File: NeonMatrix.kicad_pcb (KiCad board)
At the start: 2 copper layers, 86 x 116 mm, 40 parts, among them U1 74HC595, U2 74HC595, U3 74HC595, U4 74HC595, U5 74HC595, U6 74HC595, U7 74HC595, U8 74HC595

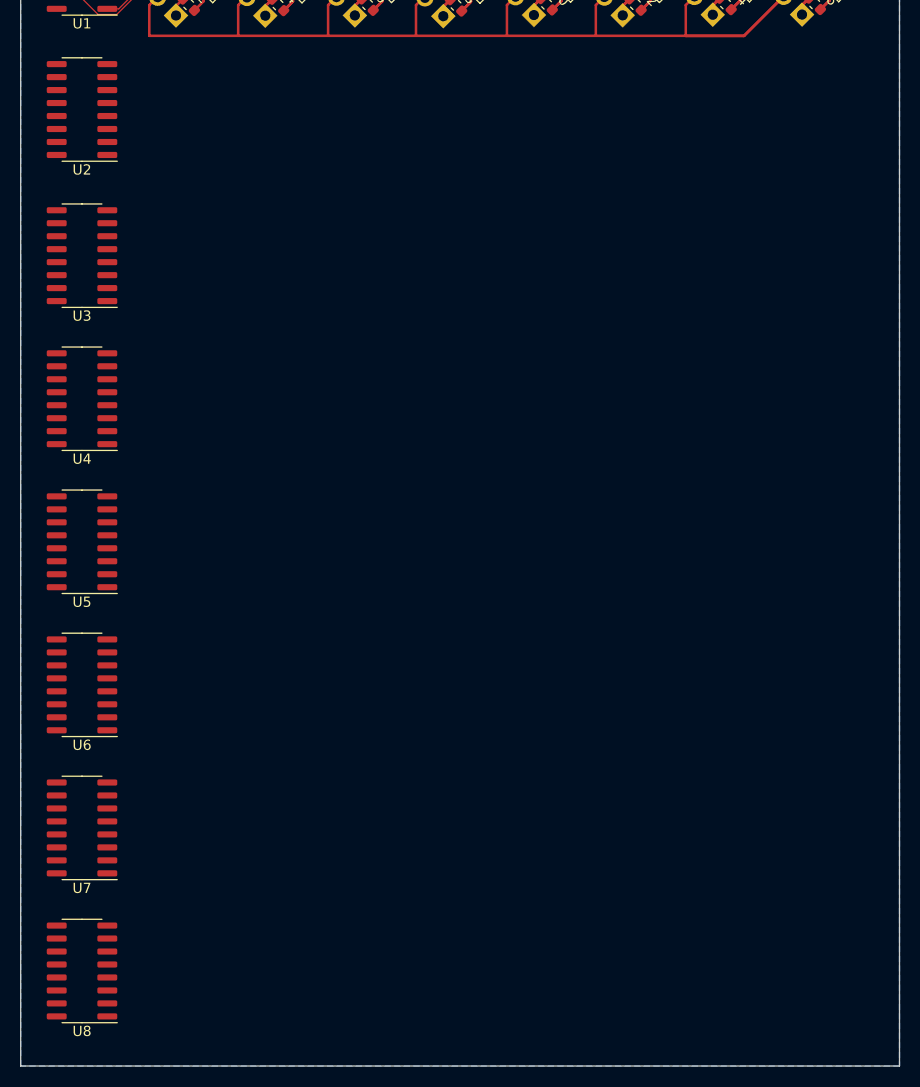
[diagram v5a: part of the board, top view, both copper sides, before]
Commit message: Add isolation
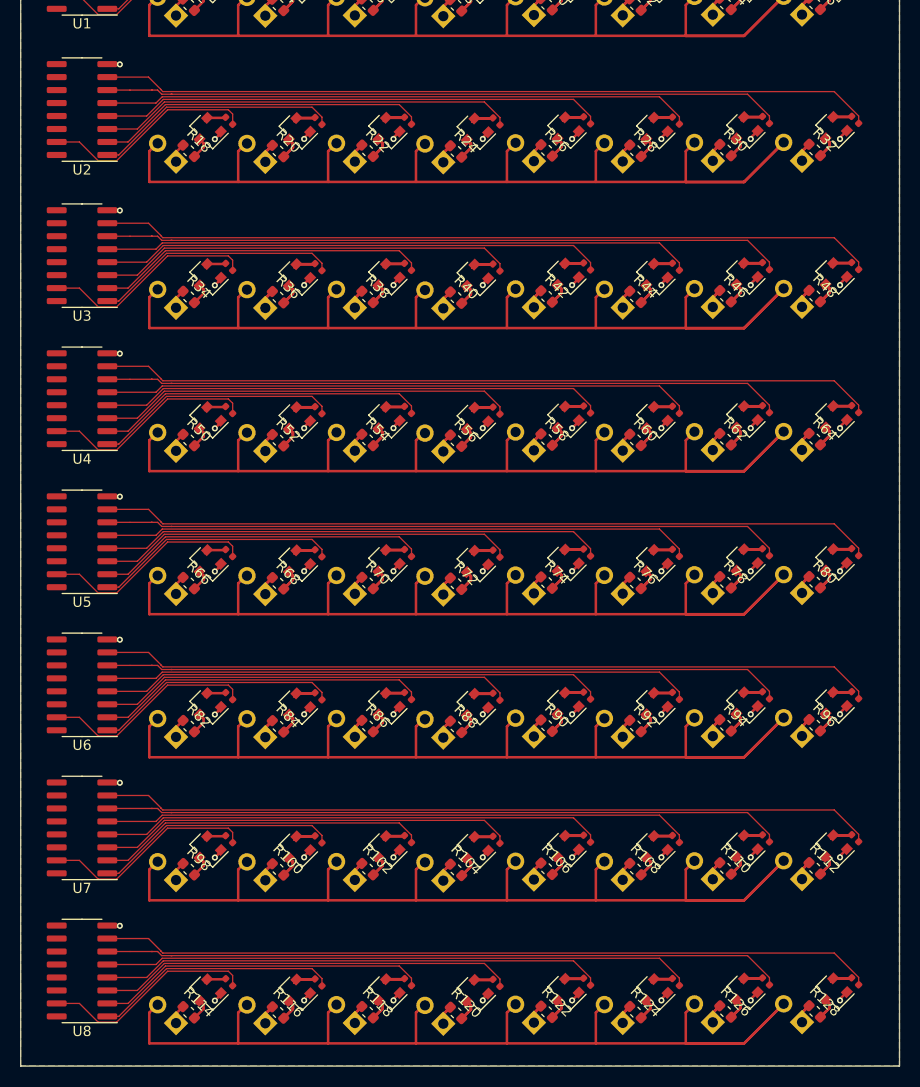
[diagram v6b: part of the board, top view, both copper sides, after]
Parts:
- added D10: Q_TRIAC_A1GA2, Package_TO_SOT_SMD:SOT-23, F.Cu at (48.9, 39.6)
- added D11: Q_TRIAC_A1GA2, Package_TO_SOT_SMD:SOT-23, F.Cu at (57.7, 39.6)
- added D12: Q_TRIAC_A1GA2, Package_TO_SOT_SMD:SOT-23, F.Cu at (66.4, 39.7)
- added D13: Q_TRIAC_A1GA2, Package_TO_SOT_SMD:SOT-23, F.Cu at (75.2, 39.5)
- added D14: Q_TRIAC_A1GA2, Package_TO_SOT_SMD:SOT-23, F.Cu at (83.9, 39.6)
- added D15: Q_TRIAC_A1GA2, Package_TO_SOT_SMD:SOT-23, F.Cu at (92.7, 39.5)
- added D16: Q_TRIAC_A1GA2, Package_TO_SOT_SMD:SOT-23, F.Cu at (101.5, 39.5)
- added D17: Q_TRIAC_A1GA2, Package_TO_SOT_SMD:SOT-23, F.Cu at (40.2, 53.9)
- added D18: Q_TRIAC_A1GA2, Package_TO_SOT_SMD:SOT-23, F.Cu at (48.9, 53.9)
- added D19: Q_TRIAC_A1GA2, Package_TO_SOT_SMD:SOT-23, F.Cu at (57.7, 53.9)
- added D20: Q_TRIAC_A1GA2, Package_TO_SOT_SMD:SOT-23, F.Cu at (66.4, 54.0)
- added D21: Q_TRIAC_A1GA2, Package_TO_SOT_SMD:SOT-23, F.Cu at (75.2, 53.8)
- added D22: Q_TRIAC_A1GA2, Package_TO_SOT_SMD:SOT-23, F.Cu at (83.9, 53.9)
- added D23: Q_TRIAC_A1GA2, Package_TO_SOT_SMD:SOT-23, F.Cu at (92.7, 53.8)
- added D24: Q_TRIAC_A1GA2, Package_TO_SOT_SMD:SOT-23, F.Cu at (101.5, 53.8)
- added D25: Q_TRIAC_A1GA2, Package_TO_SOT_SMD:SOT-23, F.Cu at (40.2, 67.9)
- added D26: Q_TRIAC_A1GA2, Package_TO_SOT_SMD:SOT-23, F.Cu at (48.9, 67.9)
- added D27: Q_TRIAC_A1GA2, Package_TO_SOT_SMD:SOT-23, F.Cu at (57.7, 67.9)
- added D28: Q_TRIAC_A1GA2, Package_TO_SOT_SMD:SOT-23, F.Cu at (66.4, 68.0)
- added D29: Q_TRIAC_A1GA2, Package_TO_SOT_SMD:SOT-23, F.Cu at (75.2, 67.8)
- added D30: Q_TRIAC_A1GA2, Package_TO_SOT_SMD:SOT-23, F.Cu at (83.9, 67.9)
- added D31: Q_TRIAC_A1GA2, Package_TO_SOT_SMD:SOT-23, F.Cu at (92.7, 67.8)
- added D32: Q_TRIAC_A1GA2, Package_TO_SOT_SMD:SOT-23, F.Cu at (101.5, 67.8)
- added D33: Q_TRIAC_A1GA2, Package_TO_SOT_SMD:SOT-23, F.Cu at (40.2, 81.9)
- added D34: Q_TRIAC_A1GA2, Package_TO_SOT_SMD:SOT-23, F.Cu at (48.9, 81.9)
- added D35: Q_TRIAC_A1GA2, Package_TO_SOT_SMD:SOT-23, F.Cu at (57.7, 81.9)
- added D36: Q_TRIAC_A1GA2, Package_TO_SOT_SMD:SOT-23, F.Cu at (66.4, 82.0)
- added D37: Q_TRIAC_A1GA2, Package_TO_SOT_SMD:SOT-23, F.Cu at (75.2, 81.8)
- added D38: Q_TRIAC_A1GA2, Package_TO_SOT_SMD:SOT-23, F.Cu at (83.9, 81.9)
- added D39: Q_TRIAC_A1GA2, Package_TO_SOT_SMD:SOT-23, F.Cu at (92.7, 81.8)
- added D40: Q_TRIAC_A1GA2, Package_TO_SOT_SMD:SOT-23, F.Cu at (101.5, 81.8)
- added D41: Q_TRIAC_A1GA2, Package_TO_SOT_SMD:SOT-23, F.Cu at (40.2, 95.9)
- added D42: Q_TRIAC_A1GA2, Package_TO_SOT_SMD:SOT-23, F.Cu at (48.9, 95.9)
- added D43: Q_TRIAC_A1GA2, Package_TO_SOT_SMD:SOT-23, F.Cu at (57.7, 95.9)
- added D44: Q_TRIAC_A1GA2, Package_TO_SOT_SMD:SOT-23, F.Cu at (66.4, 96.0)
- added D45: Q_TRIAC_A1GA2, Package_TO_SOT_SMD:SOT-23, F.Cu at (75.2, 95.8)
- added D46: Q_TRIAC_A1GA2, Package_TO_SOT_SMD:SOT-23, F.Cu at (83.9, 95.9)
- added D47: Q_TRIAC_A1GA2, Package_TO_SOT_SMD:SOT-23, F.Cu at (92.7, 95.8)
- added D48: Q_TRIAC_A1GA2, Package_TO_SOT_SMD:SOT-23, F.Cu at (101.5, 95.8)
- added D49: Q_TRIAC_A1GA2, Package_TO_SOT_SMD:SOT-23, F.Cu at (40.2, 109.9)
- added D50: Q_TRIAC_A1GA2, Package_TO_SOT_SMD:SOT-23, F.Cu at (48.9, 109.9)
- added D51: Q_TRIAC_A1GA2, Package_TO_SOT_SMD:SOT-23, F.Cu at (57.7, 109.9)
- added D52: Q_TRIAC_A1GA2, Package_TO_SOT_SMD:SOT-23, F.Cu at (66.4, 110.0)
- added D53: Q_TRIAC_A1GA2, Package_TO_SOT_SMD:SOT-23, F.Cu at (75.2, 109.8)
- added D54: Q_TRIAC_A1GA2, Package_TO_SOT_SMD:SOT-23, F.Cu at (83.9, 109.9)
- added D55: Q_TRIAC_A1GA2, Package_TO_SOT_SMD:SOT-23, F.Cu at (92.7, 109.8)
- added D56: Q_TRIAC_A1GA2, Package_TO_SOT_SMD:SOT-23, F.Cu at (101.5, 109.8)
- added D57: Q_TRIAC_A1GA2, Package_TO_SOT_SMD:SOT-23, F.Cu at (40.2, 123.9)
- added D58: Q_TRIAC_A1GA2, Package_TO_SOT_SMD:SOT-23, F.Cu at (48.9, 123.9)
- added D59: Q_TRIAC_A1GA2, Package_TO_SOT_SMD:SOT-23, F.Cu at (57.7, 123.9)
- added D60: Q_TRIAC_A1GA2, Package_TO_SOT_SMD:SOT-23, F.Cu at (66.4, 124.0)
- added D61: Q_TRIAC_A1GA2, Package_TO_SOT_SMD:SOT-23, F.Cu at (75.2, 123.8)
- added D62: Q_TRIAC_A1GA2, Package_TO_SOT_SMD:SOT-23, F.Cu at (83.9, 123.9)
- added D63: Q_TRIAC_A1GA2, Package_TO_SOT_SMD:SOT-23, F.Cu at (92.7, 123.8)
- added D64: Q_TRIAC_A1GA2, Package_TO_SOT_SMD:SOT-23, F.Cu at (101.5, 123.8)
- added D9: Q_TRIAC_A1GA2, Package_TO_SOT_SMD:SOT-23, F.Cu at (40.2, 39.6)
- added NE10: Lamp_Neon, NeonMatrix_Connector:NeonBulb, B.Cu at (45.9, 42.5)
- added NE11: Lamp_Neon, NeonMatrix_Connector:NeonBulb, B.Cu at (54.7, 42.5)
- added NE12: Lamp_Neon, NeonMatrix_Connector:NeonBulb, B.Cu at (63.4, 42.6)
- added NE13: Lamp_Neon, NeonMatrix_Connector:NeonBulb, B.Cu at (72.2, 42.5)
- added NE14: Lamp_Neon, NeonMatrix_Connector:NeonBulb, B.Cu at (80.9, 42.5)
- added NE15: Lamp_Neon, NeonMatrix_Connector:NeonBulb, B.Cu at (89.7, 42.4)
- added NE16: Lamp_Neon, NeonMatrix_Connector:NeonBulb, B.Cu at (98.5, 42.4)
- added NE17: Lamp_Neon, NeonMatrix_Connector:NeonBulb, B.Cu at (37.2, 56.8)
- added NE18: Lamp_Neon, NeonMatrix_Connector:NeonBulb, B.Cu at (45.9, 56.8)
- added NE19: Lamp_Neon, NeonMatrix_Connector:NeonBulb, B.Cu at (54.7, 56.8)
- added NE20: Lamp_Neon, NeonMatrix_Connector:NeonBulb, B.Cu at (63.4, 56.9)
- added NE21: Lamp_Neon, NeonMatrix_Connector:NeonBulb, B.Cu at (72.2, 56.8)
- added NE22: Lamp_Neon, NeonMatrix_Connector:NeonBulb, B.Cu at (80.9, 56.8)
- added NE23: Lamp_Neon, NeonMatrix_Connector:NeonBulb, B.Cu at (89.7, 56.7)
- added NE24: Lamp_Neon, NeonMatrix_Connector:NeonBulb, B.Cu at (98.5, 56.7)
- added NE25: Lamp_Neon, NeonMatrix_Connector:NeonBulb, B.Cu at (37.2, 70.8)
- added NE26: Lamp_Neon, NeonMatrix_Connector:NeonBulb, B.Cu at (45.9, 70.8)
- added NE27: Lamp_Neon, NeonMatrix_Connector:NeonBulb, B.Cu at (54.7, 70.8)
- added NE28: Lamp_Neon, NeonMatrix_Connector:NeonBulb, B.Cu at (63.4, 70.9)
- added NE29: Lamp_Neon, NeonMatrix_Connector:NeonBulb, B.Cu at (72.2, 70.8)
- added NE30: Lamp_Neon, NeonMatrix_Connector:NeonBulb, B.Cu at (80.9, 70.8)
- added NE31: Lamp_Neon, NeonMatrix_Connector:NeonBulb, B.Cu at (89.7, 70.7)
- added NE32: Lamp_Neon, NeonMatrix_Connector:NeonBulb, B.Cu at (98.5, 70.7)
- added NE33: Lamp_Neon, NeonMatrix_Connector:NeonBulb, B.Cu at (37.2, 84.8)
- added NE34: Lamp_Neon, NeonMatrix_Connector:NeonBulb, B.Cu at (45.9, 84.8)
- added NE35: Lamp_Neon, NeonMatrix_Connector:NeonBulb, B.Cu at (54.7, 84.8)
- added NE36: Lamp_Neon, NeonMatrix_Connector:NeonBulb, B.Cu at (63.4, 84.9)
- added NE37: Lamp_Neon, NeonMatrix_Connector:NeonBulb, B.Cu at (72.2, 84.8)
- added NE38: Lamp_Neon, NeonMatrix_Connector:NeonBulb, B.Cu at (80.9, 84.8)
- added NE39: Lamp_Neon, NeonMatrix_Connector:NeonBulb, B.Cu at (89.7, 84.7)
- added NE40: Lamp_Neon, NeonMatrix_Connector:NeonBulb, B.Cu at (98.5, 84.7)
- added NE41: Lamp_Neon, NeonMatrix_Connector:NeonBulb, B.Cu at (37.2, 98.8)
- added NE42: Lamp_Neon, NeonMatrix_Connector:NeonBulb, B.Cu at (45.9, 98.8)
- added NE43: Lamp_Neon, NeonMatrix_Connector:NeonBulb, B.Cu at (54.7, 98.8)
- added NE44: Lamp_Neon, NeonMatrix_Connector:NeonBulb, B.Cu at (63.4, 98.9)
- added NE45: Lamp_Neon, NeonMatrix_Connector:NeonBulb, B.Cu at (72.2, 98.8)
- added NE46: Lamp_Neon, NeonMatrix_Connector:NeonBulb, B.Cu at (80.9, 98.8)
- added NE47: Lamp_Neon, NeonMatrix_Connector:NeonBulb, B.Cu at (89.7, 98.7)
- added NE48: Lamp_Neon, NeonMatrix_Connector:NeonBulb, B.Cu at (98.5, 98.7)
- added NE49: Lamp_Neon, NeonMatrix_Connector:NeonBulb, B.Cu at (37.2, 112.8)
- added NE50: Lamp_Neon, NeonMatrix_Connector:NeonBulb, B.Cu at (45.9, 112.8)
- added NE51: Lamp_Neon, NeonMatrix_Connector:NeonBulb, B.Cu at (54.7, 112.8)
- added NE52: Lamp_Neon, NeonMatrix_Connector:NeonBulb, B.Cu at (63.4, 112.9)
- added NE53: Lamp_Neon, NeonMatrix_Connector:NeonBulb, B.Cu at (72.2, 112.8)
- added NE54: Lamp_Neon, NeonMatrix_Connector:NeonBulb, B.Cu at (80.9, 112.8)
- added NE55: Lamp_Neon, NeonMatrix_Connector:NeonBulb, B.Cu at (89.7, 112.7)
- added NE56: Lamp_Neon, NeonMatrix_Connector:NeonBulb, B.Cu at (98.5, 112.7)
- added NE57: Lamp_Neon, NeonMatrix_Connector:NeonBulb, B.Cu at (37.2, 126.8)
- added NE58: Lamp_Neon, NeonMatrix_Connector:NeonBulb, B.Cu at (45.9, 126.8)
- added NE59: Lamp_Neon, NeonMatrix_Connector:NeonBulb, B.Cu at (54.7, 126.8)
- added NE60: Lamp_Neon, NeonMatrix_Connector:NeonBulb, B.Cu at (63.4, 126.9)
- added NE61: Lamp_Neon, NeonMatrix_Connector:NeonBulb, B.Cu at (72.2, 126.8)
- added NE62: Lamp_Neon, NeonMatrix_Connector:NeonBulb, B.Cu at (80.9, 126.8)
- added NE63: Lamp_Neon, NeonMatrix_Connector:NeonBulb, B.Cu at (89.7, 126.7)
- added NE64: Lamp_Neon, NeonMatrix_Connector:NeonBulb, B.Cu at (98.5, 126.7)
- added NE9: Lamp_Neon, NeonMatrix_Connector:NeonBulb, B.Cu at (37.2, 42.5)
- added R100: 33k, Resistor_SMD:R_0603_1608Metric, F.Cu at (47.2, 111.8)
- added R101: 330k, Resistor_SMD:R_0402_1005Metric, F.Cu at (59.9, 108.8)
- added R102: 33k, Resistor_SMD:R_0603_1608Metric, F.Cu at (55.9, 111.7)
- added R103: 330k, Resistor_SMD:R_0402_1005Metric, F.Cu at (68.6, 108.9)
- added R104: 33k, Resistor_SMD:R_0603_1608Metric, F.Cu at (64.6, 111.8)
- added R105: 330k, Resistor_SMD:R_0402_1005Metric, F.Cu at (77.4, 108.8)
- added R106: 33k, Resistor_SMD:R_0603_1608Metric, F.Cu at (73.5, 111.7)
- added R107: 330k, Resistor_SMD:R_0402_1005Metric, F.Cu at (86.1, 108.8)
- added R108: 33k, Resistor_SMD:R_0603_1608Metric, F.Cu at (82.2, 111.7)
- added R109: 330k, Resistor_SMD:R_0402_1005Metric, F.Cu at (94.9, 108.7)
- added R110: 33k, Resistor_SMD:R_0603_1608Metric, F.Cu at (91.0, 111.7)
- added R111: 330k, Resistor_SMD:R_0402_1005Metric, F.Cu at (103.7, 108.7)
- added R112: 33k, Resistor_SMD:R_0603_1608Metric, F.Cu at (99.7, 111.7)
- added R113: 330k, Resistor_SMD:R_0402_1005Metric, F.Cu at (42.4, 122.8)
- added R114: 33k, Resistor_SMD:R_0603_1608Metric, F.Cu at (38.4, 125.7)
- added R115: 330k, Resistor_SMD:R_0402_1005Metric, F.Cu at (51.1, 122.8)
- added R116: 33k, Resistor_SMD:R_0603_1608Metric, F.Cu at (47.2, 125.8)
- added R117: 330k, Resistor_SMD:R_0402_1005Metric, F.Cu at (59.9, 122.8)
- added R118: 33k, Resistor_SMD:R_0603_1608Metric, F.Cu at (55.9, 125.7)
- added R119: 330k, Resistor_SMD:R_0402_1005Metric, F.Cu at (68.6, 122.9)
- added R120: 33k, Resistor_SMD:R_0603_1608Metric, F.Cu at (64.6, 125.8)
- added R121: 330k, Resistor_SMD:R_0402_1005Metric, F.Cu at (77.4, 122.8)
- added R122: 33k, Resistor_SMD:R_0603_1608Metric, F.Cu at (73.5, 125.7)
- added R123: 330k, Resistor_SMD:R_0402_1005Metric, F.Cu at (86.1, 122.8)
- added R124: 33k, Resistor_SMD:R_0603_1608Metric, F.Cu at (82.2, 125.7)
- added R125: 330k, Resistor_SMD:R_0402_1005Metric, F.Cu at (94.9, 122.7)
- added R126: 33k, Resistor_SMD:R_0603_1608Metric, F.Cu at (91.0, 125.7)
- added R127: 330k, Resistor_SMD:R_0402_1005Metric, F.Cu at (103.7, 122.7)
- added R128: 33k, Resistor_SMD:R_0603_1608Metric, F.Cu at (99.7, 125.7)
- added R17: 330k, Resistor_SMD:R_0402_1005Metric, F.Cu at (42.4, 38.5)
- added R18: 33k, Resistor_SMD:R_0603_1608Metric, F.Cu at (38.4, 41.4)
- added R19: 330k, Resistor_SMD:R_0402_1005Metric, F.Cu at (51.1, 38.5)
- added R20: 33k, Resistor_SMD:R_0603_1608Metric, F.Cu at (47.2, 41.5)
- added R21: 330k, Resistor_SMD:R_0402_1005Metric, F.Cu at (59.9, 38.5)
- added R22: 33k, Resistor_SMD:R_0603_1608Metric, F.Cu at (55.9, 41.4)
- added R23: 330k, Resistor_SMD:R_0402_1005Metric, F.Cu at (68.6, 38.6)
- added R24: 33k, Resistor_SMD:R_0603_1608Metric, F.Cu at (64.6, 41.5)
- added R25: 330k, Resistor_SMD:R_0402_1005Metric, F.Cu at (77.4, 38.5)
- added R26: 33k, Resistor_SMD:R_0603_1608Metric, F.Cu at (73.5, 41.4)
- added R27: 330k, Resistor_SMD:R_0402_1005Metric, F.Cu at (86.1, 38.5)
- added R28: 33k, Resistor_SMD:R_0603_1608Metric, F.Cu at (82.2, 41.4)
- added R29: 330k, Resistor_SMD:R_0402_1005Metric, F.Cu at (94.9, 38.4)
- added R30: 33k, Resistor_SMD:R_0603_1608Metric, F.Cu at (91.0, 41.4)
- added R31: 330k, Resistor_SMD:R_0402_1005Metric, F.Cu at (103.7, 38.4)
- added R32: 33k, Resistor_SMD:R_0603_1608Metric, F.Cu at (99.7, 41.4)
- added R33: 330k, Resistor_SMD:R_0402_1005Metric, F.Cu at (42.4, 52.8)
- added R34: 33k, Resistor_SMD:R_0603_1608Metric, F.Cu at (38.4, 55.7)
- added R35: 330k, Resistor_SMD:R_0402_1005Metric, F.Cu at (51.1, 52.8)
- added R36: 33k, Resistor_SMD:R_0603_1608Metric, F.Cu at (47.2, 55.8)
- added R37: 330k, Resistor_SMD:R_0402_1005Metric, F.Cu at (59.9, 52.8)
- added R38: 33k, Resistor_SMD:R_0603_1608Metric, F.Cu at (55.9, 55.7)
- added R39: 330k, Resistor_SMD:R_0402_1005Metric, F.Cu at (68.6, 52.9)
- added R40: 33k, Resistor_SMD:R_0603_1608Metric, F.Cu at (64.6, 55.8)
- added R41: 330k, Resistor_SMD:R_0402_1005Metric, F.Cu at (77.4, 52.8)
- added R42: 33k, Resistor_SMD:R_0603_1608Metric, F.Cu at (73.5, 55.7)
- added R43: 330k, Resistor_SMD:R_0402_1005Metric, F.Cu at (86.1, 52.8)
- added R44: 33k, Resistor_SMD:R_0603_1608Metric, F.Cu at (82.2, 55.7)
- added R45: 330k, Resistor_SMD:R_0402_1005Metric, F.Cu at (94.9, 52.7)
- added R46: 33k, Resistor_SMD:R_0603_1608Metric, F.Cu at (91.0, 55.7)
- added R47: 330k, Resistor_SMD:R_0402_1005Metric, F.Cu at (103.7, 52.7)
- added R48: 33k, Resistor_SMD:R_0603_1608Metric, F.Cu at (99.7, 55.7)
- added R49: 330k, Resistor_SMD:R_0402_1005Metric, F.Cu at (42.4, 66.8)
- added R50: 33k, Resistor_SMD:R_0603_1608Metric, F.Cu at (38.4, 69.7)
- added R51: 330k, Resistor_SMD:R_0402_1005Metric, F.Cu at (51.1, 66.8)
- added R52: 33k, Resistor_SMD:R_0603_1608Metric, F.Cu at (47.2, 69.8)
- added R53: 330k, Resistor_SMD:R_0402_1005Metric, F.Cu at (59.9, 66.8)
- added R54: 33k, Resistor_SMD:R_0603_1608Metric, F.Cu at (55.9, 69.7)
- added R55: 330k, Resistor_SMD:R_0402_1005Metric, F.Cu at (68.6, 66.9)
- added R56: 33k, Resistor_SMD:R_0603_1608Metric, F.Cu at (64.6, 69.8)
- added R57: 330k, Resistor_SMD:R_0402_1005Metric, F.Cu at (77.4, 66.8)
- added R58: 33k, Resistor_SMD:R_0603_1608Metric, F.Cu at (73.5, 69.7)
- added R59: 330k, Resistor_SMD:R_0402_1005Metric, F.Cu at (86.1, 66.8)
- added R60: 33k, Resistor_SMD:R_0603_1608Metric, F.Cu at (82.2, 69.7)
- added R61: 330k, Resistor_SMD:R_0402_1005Metric, F.Cu at (94.9, 66.7)
- added R62: 33k, Resistor_SMD:R_0603_1608Metric, F.Cu at (91.0, 69.7)
- added R63: 330k, Resistor_SMD:R_0402_1005Metric, F.Cu at (103.7, 66.7)
- added R64: 33k, Resistor_SMD:R_0603_1608Metric, F.Cu at (99.7, 69.7)
- added R65: 330k, Resistor_SMD:R_0402_1005Metric, F.Cu at (42.4, 80.8)
- added R66: 33k, Resistor_SMD:R_0603_1608Metric, F.Cu at (38.4, 83.7)
- added R67: 330k, Resistor_SMD:R_0402_1005Metric, F.Cu at (51.1, 80.8)
- added R68: 33k, Resistor_SMD:R_0603_1608Metric, F.Cu at (47.2, 83.8)
- added R69: 330k, Resistor_SMD:R_0402_1005Metric, F.Cu at (59.9, 80.8)
- added R70: 33k, Resistor_SMD:R_0603_1608Metric, F.Cu at (55.9, 83.7)
- added R71: 330k, Resistor_SMD:R_0402_1005Metric, F.Cu at (68.6, 80.9)
- added R72: 33k, Resistor_SMD:R_0603_1608Metric, F.Cu at (64.6, 83.8)
- added R73: 330k, Resistor_SMD:R_0402_1005Metric, F.Cu at (77.4, 80.8)
- added R74: 33k, Resistor_SMD:R_0603_1608Metric, F.Cu at (73.5, 83.7)
- added R75: 330k, Resistor_SMD:R_0402_1005Metric, F.Cu at (86.1, 80.8)
- added R76: 33k, Resistor_SMD:R_0603_1608Metric, F.Cu at (82.2, 83.7)
- added R77: 330k, Resistor_SMD:R_0402_1005Metric, F.Cu at (94.9, 80.7)
- added R78: 33k, Resistor_SMD:R_0603_1608Metric, F.Cu at (91.0, 83.7)
- added R79: 330k, Resistor_SMD:R_0402_1005Metric, F.Cu at (103.7, 80.7)
- added R80: 33k, Resistor_SMD:R_0603_1608Metric, F.Cu at (99.7, 83.7)
- added R81: 330k, Resistor_SMD:R_0402_1005Metric, F.Cu at (42.4, 94.8)
- added R82: 33k, Resistor_SMD:R_0603_1608Metric, F.Cu at (38.4, 97.7)
- added R83: 330k, Resistor_SMD:R_0402_1005Metric, F.Cu at (51.1, 94.8)
- added R84: 33k, Resistor_SMD:R_0603_1608Metric, F.Cu at (47.2, 97.8)
- added R85: 330k, Resistor_SMD:R_0402_1005Metric, F.Cu at (59.9, 94.8)
- added R86: 33k, Resistor_SMD:R_0603_1608Metric, F.Cu at (55.9, 97.7)
- added R87: 330k, Resistor_SMD:R_0402_1005Metric, F.Cu at (68.6, 94.9)
- added R88: 33k, Resistor_SMD:R_0603_1608Metric, F.Cu at (64.6, 97.8)
- added R89: 330k, Resistor_SMD:R_0402_1005Metric, F.Cu at (77.4, 94.8)
- added R90: 33k, Resistor_SMD:R_0603_1608Metric, F.Cu at (73.5, 97.7)
- added R91: 330k, Resistor_SMD:R_0402_1005Metric, F.Cu at (86.1, 94.8)
- added R92: 33k, Resistor_SMD:R_0603_1608Metric, F.Cu at (82.2, 97.7)
- added R93: 330k, Resistor_SMD:R_0402_1005Metric, F.Cu at (94.9, 94.7)
- added R94: 33k, Resistor_SMD:R_0603_1608Metric, F.Cu at (91.0, 97.7)
- added R95: 330k, Resistor_SMD:R_0402_1005Metric, F.Cu at (103.7, 94.7)
- added R96: 33k, Resistor_SMD:R_0603_1608Metric, F.Cu at (99.7, 97.7)
- added R97: 330k, Resistor_SMD:R_0402_1005Metric, F.Cu at (42.4, 108.8)
- added R98: 33k, Resistor_SMD:R_0603_1608Metric, F.Cu at (38.4, 111.7)
- added R99: 330k, Resistor_SMD:R_0402_1005Metric, F.Cu at (51.1, 108.8)
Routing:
- net LINE: track 104.4 -> 834.8 mm
- net /sheet5EFA9519/sheet5EF2B9F4/SIGNAL: track 0.00 -> 75.8 mm
- net /sheet5EFAAFC6/sheet5EF2B9F4/SIGNAL: track 0.00 -> 75.8 mm
- net /sheet5EFAAFC5/sheet5EF2B9F4/SIGNAL: track 0.00 -> 75.8 mm
- net /sheet5EFAAFC4/sheet5EF2B9F4/SIGNAL: track 0.00 -> 75.8 mm
- net /sheet5EFAAFC3/sheet5EF2B9F4/SIGNAL: track 0.00 -> 75.8 mm
- net /sheet5EFA93E5/sheet5EF2B9F4/SIGNAL: track 0.00 -> 75.8 mm
- net /sheet5EFA929F/sheet5EF2B9F4/SIGNAL: track 0.00 -> 75.8 mm
- net /sheet5EFA93E5/sheet5EF2B938/SIGNAL: track 0.00 -> 66.8 mm
- net /sheet5EFA929F/sheet5EF2B938/SIGNAL: track 0.00 -> 66.8 mm
- net /sheet5EFAAFC6/sheet5EF2B938/SIGNAL: track 0.00 -> 66.8 mm
- net /sheet5EFAAFC5/sheet5EF2B938/SIGNAL: track 0.00 -> 66.8 mm
- net /sheet5EFAAFC4/sheet5EF2B938/SIGNAL: track 0.00 -> 66.8 mm
- net /sheet5EFAAFC3/sheet5EF2B938/SIGNAL: track 0.00 -> 66.8 mm
- net /sheet5EFA9519/sheet5EF2B938/SIGNAL: track 0.00 -> 66.8 mm
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
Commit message: Add routing
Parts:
- added C1: 100n, Capacitor_SMD:C_0805_2012Metric, F.Cu at (162.1, 49.0)
- added C10: 100n, Capacitor_SMD:C_0805_2012Metric, F.Cu at (183.7, 103.4)
- added C11: 100n, Capacitor_SMD:C_0805_2012Metric, F.Cu at (183.9, 61.4)
- added C12: 100n, Capacitor_SMD:C_0805_2012Metric, F.Cu at (183.8, 89.4)
- added C13: 100n, Capacitor_SMD:C_0805_2012Metric, F.Cu at (183.6, 75.3)
- added C2: 100n, Capacitor_SMD:C_0805_2012Metric, F.Cu at (162.0, 58.0)
- added C3: 100n, Capacitor_SMD:C_0805_2012Metric, F.Cu at (169.5, 58.0)
- added C4: 100n, Capacitor_SMD:C_0805_2012Metric, F.Cu at (169.5, 49.0)
- added C5: 22u, Capacitor_SMD:C_0805_2012Metric, F.Cu at (169.5, 44.5)
- added C6: 100n, Capacitor_SMD:C_0805_2012Metric, F.Cu at (183.6, 131.4)
- added C7: 100n, Capacitor_SMD:C_0805_2012Metric, F.Cu at (183.8, 32.6)
- added C8: 100n, Capacitor_SMD:C_0805_2012Metric, F.Cu at (183.6, 117.4)
- added C9: 100n, Capacitor_SMD:C_0805_2012Metric, F.Cu at (184.0, 47.1)
- added J1: Mains, TerminalBlock_RND:TerminalBlock_RND_205-00001_1x02_P5.00mm_Horizontal, F.Cu at (157.0, 139.5)
- added J2: Data, Connector_PinHeader_2.54mm:PinHeader_1x06_P2.54mm_Vertical, F.Cu at (151.5, 51.0)
- added M1: B0505S, NeonMatrix:M_DCDC_SIP4, F.Cu at (165.6, 41.5)
- added U10: ADuM1200AR, Package_SO:SOIC-8_3.9x4.9mm_P1.27mm, F.Cu at (166.0, 62.0)
- added U9: ADuM1200AR, Package_SO:SOIC-8_3.9x4.9mm_P1.27mm, F.Cu at (166.0, 53.0)
- R1, R101, R103, R105, R107, R109, R11, R111, R113, R115, R117, R119, R121, R123, R125, R127, R13, R15, R17, R19, R21, R23, R25, R27, R29, R3, R31, R33, R35, R37, R39, R41, R43, R45, R47, R49, R5, R51, R53, R55, R57, R59, R61, R63, R65, R67, R69, R7, R71, R73, R75, R77, R79, R81, R83, R85, R87, R89, R9, R91, R93, R95, R97, R99: value 330k -> 33k
- moved D1 156.8 mm to (196.2, 41.3)
- moved D10 156.8 mm to (204.9, 55.6)
- moved D11 156.8 mm to (213.7, 55.6)
- moved D12 156.8 mm to (222.4, 55.6)
- moved D13 156.8 mm to (231.2, 55.5)
- moved D14 156.8 mm to (239.9, 55.6)
- moved D15 156.8 mm to (248.7, 55.5)
- moved D16 156.8 mm to (257.5, 55.5)
- moved D17 156.8 mm to (196.2, 69.9)
- moved D18 156.8 mm to (204.9, 69.9)
- moved D19 156.8 mm to (213.7, 69.9)
- moved D2 156.8 mm to (204.9, 41.3)
- moved D20 156.8 mm to (222.4, 69.9)
- moved D21 156.8 mm to (231.2, 69.8)
- moved D22 156.8 mm to (239.9, 69.9)
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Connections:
- U1 pad 14: /Sheet595Neon/DATAIN -> /DATAIN
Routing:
- net LINE: track 834.8 -> 1070.2 mm
- net +3V3: track 0.00 -> 186.5 mm, vias 0 -> 16
- net /OE: track 0.00 -> 179.4 mm, vias 0 -> 9
- net /LATCH: track 0.00 -> 168.3 mm, vias 0 -> 9
- net /SCK: track 0.00 -> 156.4 mm, vias 0 -> 9
- net /sheet5EFA929F/DATAIN: track 0.00 -> 37.9 mm, vias 0 -> 2
- net /ISO_5V: track 0.00 -> 37.4 mm
- net /sheet5EFAAFC3/DATAIN: track 0.00 -> 29.6 mm, vias 0 -> 2
- net /sheet5EFAAFC6/DATAIN: track 0.00 -> 29.4 mm, vias 0 -> 2
- net /sheet5EFAAFC5/DATAIN: track 0.00 -> 28.8 mm, vias 0 -> 2
- net /sheet5EFAAFC4/DATAIN: track 0.00 -> 28.5 mm, vias 0 -> 2
- net /sheet5EFA9519/DATAIN: track 0.00 -> 27.9 mm, vias 0 -> 2
- net /sheet5EFA93E5/DATAIN: track 0.00 -> 27.3 mm, vias 0 -> 2
- net /DATAIN: track 0.00 -> 23.0 mm, vias 0 -> 2
- net /ISO_SCK: track 0.00 -> 14.1 mm
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- added copper zone on B.Cu, net /ISO_GND
- added copper zone on F.Cu, net /ISO_GND
- added copper zone on F.Cu, net GND
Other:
- board size 86 x 116 mm -> 116 x 116 mm

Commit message: Add labels to connectors
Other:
- board text added: "DATAIN"
- board text added: "GND"
- board text added: "JLCJLCJLCJLC"
- board text added: "LATCH"
- board text added: "LINE"
- board text added: "NEUTRAL"
- board text added: "OE"
- board text added: "SCK"
- board text added: "VCC"
